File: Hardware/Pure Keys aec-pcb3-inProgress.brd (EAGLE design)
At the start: 99 x 98.7 mm, 61 parts, among them IC1 MCP6004P, IC5 MCP6004P, Q2 20MHz, T1 2N3904, U2 LM4040, U3 328P

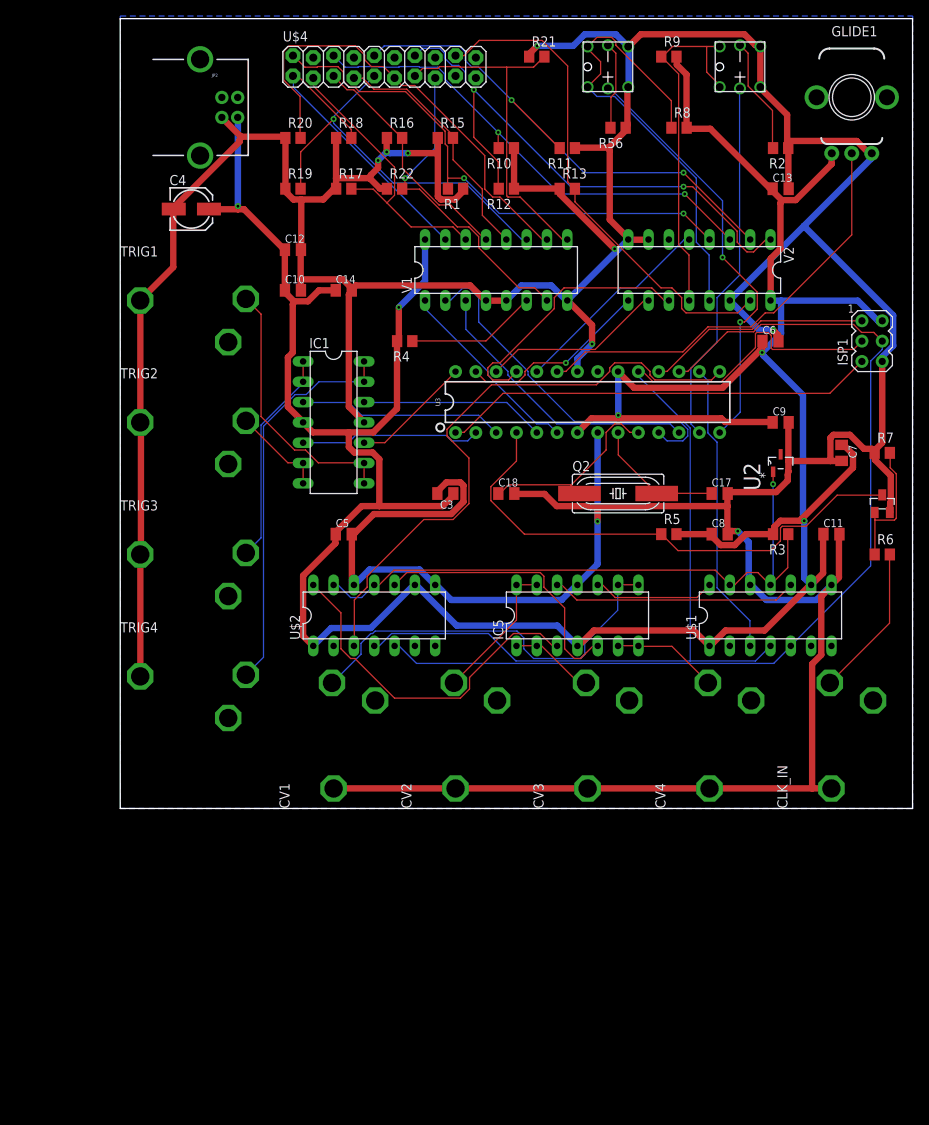
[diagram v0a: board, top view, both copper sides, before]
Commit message: adding part numbers to attributes
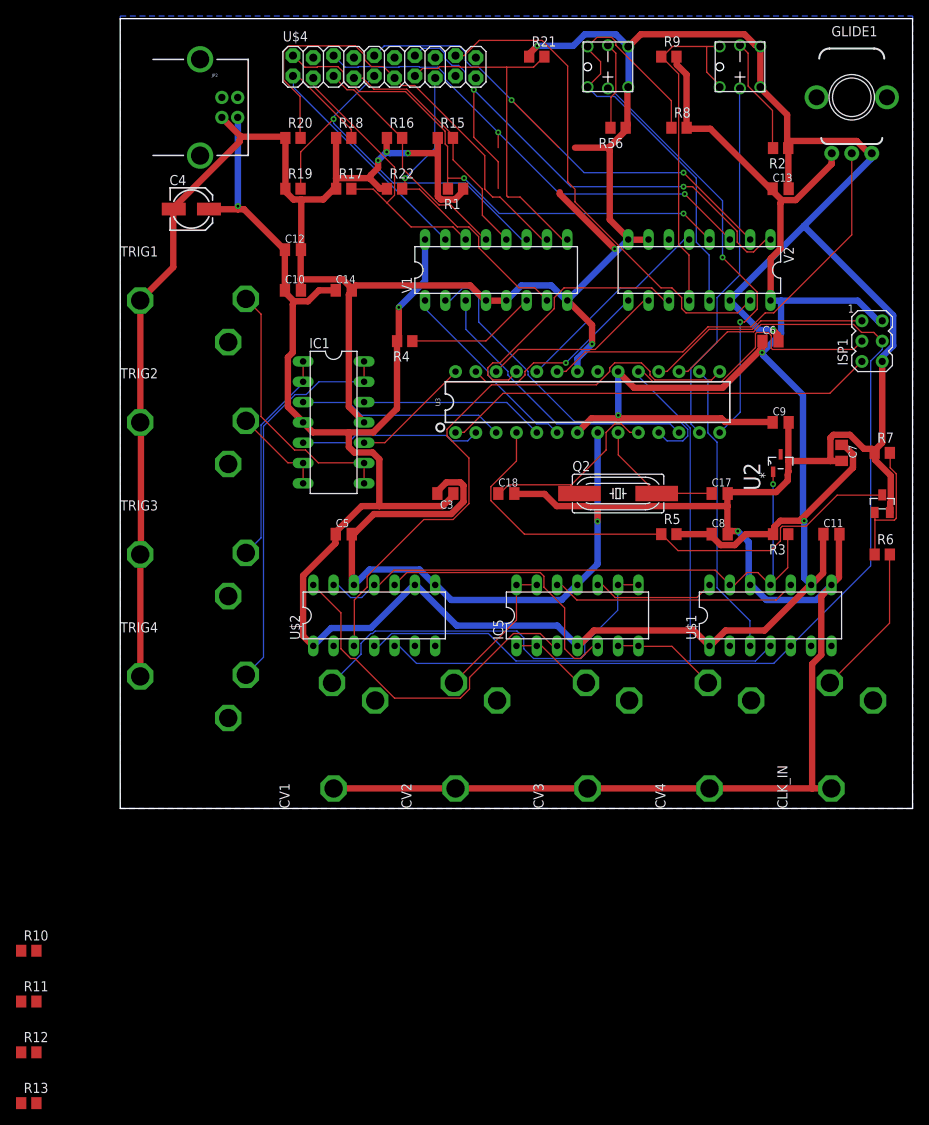
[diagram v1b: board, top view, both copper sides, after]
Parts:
- moved R13 132.6 mm to (-11.4, -36.8)
- moved R11 126.1 mm to (-11.4, -24.1), turned to 0 degrees
- moved R12 123.4 mm to (-11.4, -30.5), turned to 0 degrees
- moved R10 116.7 mm to (-11.4, -17.8), turned to 0 degrees
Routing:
- net GND: track 674.9 -> 663.6 mm
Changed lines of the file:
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@@
 <attribute name="OC_NEWARK" value="58K5870" x="82.55" y="43.18" size="1.778" layer="27" rot="R90" display="off"/>
 <attribute name="PACKAGE" value="3-SOT-23" x="82.55" y="43.18" size="1.778" layer="27" rot="R90" display="off"/>
+<attribute name="RS-PART" value="809-6343" x="82.55" y="43.18" size="1.778" layer="27" rot="R90" display="off"/>
 <attribute name="SUPPLIER" value="TEXAS INSTRUMENTS" x="82.55" y="43.18" size="1.778" layer="27" rot="R90" display="off"/>
 </element>
@@
 <element name="R8" library="rcl" package="R0805" value="100K" x="69.85" y="85.09"/>
 <element name="R9" library="rcl" package="R0805" value="100K" x="68.58" y="93.98"/>
-<element name="R1" library="rcl" package="R0805" value="1K" x="41.91" y="77.47" rot="R180"/>
-<element name="R10" library="rcl" package="R0805" value="1K" x="48.26" y="82.55" rot="R180"/>
-<element name="R11" library="rcl" package="R0805" value="1K" x="55.88" y="82.55" rot="R180"/>
-<element name="R12" library="rcl" package="R0805" value="1K" x="48.26" y="77.47" rot="R180"/>
-<element name="R13" library="rcl" package="R0805" value="1K" x="55.88" y="77.47"/>
+<element name="R1" library="rcl" package="R0805" value="1K" x="41.91" y="77.47" rot="R180">
+<attribute name="RS-PART" value="223-0427" x="41.91" y="77.47" size="1.778" layer="27" rot="R180" display="off"/>
+</element>
+<element name="R10" library="rcl" package="R0805" value="1K" x="-11.43" y="-17.78">
+<attribute name="RS-PART" value="223-0427" x="-11.43" y="-17.78" size="1.778" layer="27" display="off"/>
+</element>
+<element name="R11" library="rcl" package="R0805" value="1K" x="-11.43" y="-24.13">
+<attribute name="RS-PART" value="223-0427" x="-11.43" y="-24.13" size="1.778" layer="27" display="off"/>
+</element>
+<element name="R12" library="rcl" package="R0805" value="1K" x="-11.43" y="-30.48">
+<attribute name="RS-PART" value="223-0427" x="-11.43" y="-30.48" size="1.778" layer="27" display="off"/>
+</element>
+<element name="R13" library="rcl" package="R0805" value="1K" x="-11.43" y="-36.83">
+<attribute name="RS-PART" value="223-0427" x="-11.43" y="-36.83" size="1.778" layer="27" display="off"/>
+</element>
 </elements>
 <signals>
@@
 <contactref element="BUT2" pad="2"/>
 <contactref element="R1" pad="1"/>
-<contactref element="R10" pad="1"/>
-<contactref element="R11" pad="1"/>
-<contactref element="R12" pad="1"/>
-<contactref element="R13" pad="1"/>
 <wire x1="41.91" y1="2.5146" x2="26.67" y2="2.5146" width="0.8" layer="1"/>
 <wire x1="26.67" y1="2.5146" x2="26.67" y2="2.5" width="0.8" layer="1"/>
@@
 <wire x1="63.1698" y1="84.7344" x2="61.0362" y2="82.6008" width="0.8" layer="1"/>
 <wire x1="63.1698" y1="85.0392" x2="63.1698" y2="84.7344" width="0.8" layer="1"/>
-<wire x1="56.8452" y1="82.6008" x2="56.83" y2="82.55" width="0.8" layer="1"/>
 <wire x1="63.1698" y1="85.0392" x2="63.18" y2="85.09" width="0.8" layer="1"/>
 <wire x1="51.1302" y1="94.3356" x2="51.1302" y2="94.0308" width="0.8" layer="1"/>
@@
 <wire x1="63.5" y1="90.17" x2="63.3984" y2="90.0684" width="0.8" layer="1"/>
 <wire x1="63.3984" y1="85.4202" x2="63.18" y2="85.09" width="0.8" layer="1"/>
-<wire x1="49.2252" y1="82.5246" x2="49.2252" y2="77.4954" width="0.8" layer="1"/>
-<wire x1="49.2252" y1="77.4954" x2="49.21" y2="77.47" width="0.8" layer="1"/>
-<wire x1="49.2252" y1="82.5246" x2="49.21" y2="82.55" width="0.8" layer="1"/>
-<wire x1="49.6062" y1="77.4954" x2="54.864" y2="77.4954" width="0.8" layer="1"/>
-<wire x1="54.864" y1="77.4954" x2="54.93" y2="77.47" width="0.8" layer="1"/>
-<wire x1="49.6062" y1="77.4954" x2="49.21" y2="77.47" width="0.8" layer="1"/>
 <wire x1="65.9892" y1="71.0946" x2="63.5508" y2="71.0946" width="0.8" layer="1"/>
 <wire x1="63.5508" y1="71.0946" x2="63.5" y2="71.12" width="0.8" layer="1"/>
@@
 <wire x1="54.9402" y1="76.8096" x2="54.9402" y2="77.0382" width="0.8" layer="1"/>
 <wire x1="61.7982" y1="69.9516" x2="54.9402" y2="76.8096" width="0.8" layer="1"/>
-<wire x1="54.9402" y1="77.0382" x2="54.93" y2="77.47" width="0.8" layer="1"/>
 <wire x1="61.7982" y1="69.9516" x2="62.0649" y2="69.6849" width="0.8" layer="16"/>
 <wire x1="61.1886" y1="73.6092" x2="61.1886" y2="82.2198" width="0.8" layer="1"/>
@@
 <via x="32.2326" y="81.0006" extent="1-16" drill="0.35"/>
 <via x="35.9664" y="81.915" extent="1-16" drill="0.35"/>
+<contactref element="R10" pad="1"/>
+<contactref element="R11" pad="1"/>
+<contactref element="R12" pad="1"/>
+<contactref element="R13" pad="1"/>
+<wire x1="-12.38" y1="-30.48" x2="-12.38" y2="-36.83" width="0" layer="19" extent="1-1"/>
+<wire x1="-12.38" y1="-24.13" x2="-12.38" y2="-30.48" width="0" layer="19" extent="1-1"/>
+<wire x1="-12.38" y1="-17.78" x2="-12.38" y2="-24.13" width="0" layer="19" extent="1-1"/>
+<wire x1="2.5" y1="16.51" x2="-12.38" y2="-17.78" width="0" layer="19" extent="1-1"/>
 </signal>
 <signal name="RST">
@@
 <contactref element="V2" pad="15"/>
 <contactref element="U$4" pad="18"/>
-<contactref element="R13" pad="2"/>
 <wire x1="56.8452" y1="75.819" x2="56.8452" y2="77.4192" width="0.1524" layer="1"/>
 <wire x1="67.5894" y1="65.0748" x2="56.8452" y2="75.819" width="0.1524" layer="1"/>
@@
 <wire x1="77.1906" y1="61.9506" x2="70.7136" y2="61.9506" width="0.1524" layer="1"/>
 <wire x1="78.74" y1="63.5" x2="77.1906" y2="61.9506" width="0.1524" layer="1"/>
-<wire x1="56.8452" y1="77.4192" x2="56.83" y2="77.47" width="0.1524" layer="1"/>
 <wire x1="42.9768" y1="94.107" x2="41.91" y2="94.107" width="0.1524" layer="1"/>
 <wire x1="44.8818" y1="96.012" x2="42.9768" y2="94.107" width="0.1524" layer="1"/>
@@
 <wire x1="55.9308" y1="78.3336" x2="55.9308" y2="92.8116" width="0.1524" layer="1"/>
 <wire x1="56.769" y1="77.4954" x2="55.9308" y2="78.3336" width="0.1524" layer="1"/>
-<wire x1="56.769" y1="77.4954" x2="56.83" y2="77.47" width="0.1524" layer="1"/>
+<contactref element="R13" pad="2"/>
+<wire x1="56.8452" y1="77.4192" x2="56.769" y2="77.4954" width="0" layer="19" extent="1-1"/>
+<wire x1="-10.48" y1="-36.83" x2="70.7136" y2="61.9506" width="0" layer="19" extent="1-1"/>
 </signal>
 <signal name="MK3">
 <contactref element="U$4" pad="14"/>
-<contactref element="R12" pad="2"/>
 <contactref element="V2" pad="1"/>
 <wire x1="47.244" y1="80.8482" x2="47.244" y2="77.4954" width="0.1524" layer="1"/>
@@
 <wire x1="37.7952" y1="95.0214" x2="39.9288" y2="95.0214" width="0.1524" layer="16"/>
 <wire x1="36.8808" y1="94.107" x2="37.7952" y2="95.0214" width="0.1524" layer="16"/>
-<wire x1="47.244" y1="77.4954" x2="47.31" y2="77.47" width="0.1524" layer="1"/>
 <wire x1="36.8808" y1="94.107" x2="36.83" y2="94.107" width="0.1524" layer="16"/>
 <wire x1="80.6958" y1="71.0946" x2="81.2292" y2="71.0946" width="0.1524" layer="1"/>
@@
 <via x="44.196" y="89.8398" extent="1-16" drill="0.35"/>
 <via x="70.4088" y="77.724" extent="1-16" drill="0.35"/>
+<contactref element="R12" pad="2"/>
+<wire x1="-10.48" y1="-30.48" x2="47.244" y2="77.4954" width="0" layer="19" extent="1-1"/>
 </signal>
 <signal name="MK2">
 <contactref element="U$4" pad="10"/>
-<contactref element="R11" pad="2"/>
 <contactref element="V2" pad="2"/>
 <wire x1="48.9204" y1="88.5444" x2="54.864" y2="82.6008" width="0.1524" layer="1"/>
@@
 <wire x1="32.9946" y1="95.3262" x2="42.3672" y2="95.3262" width="0.1524" layer="16"/>
 <wire x1="31.7754" y1="94.107" x2="32.9946" y2="95.3262" width="0.1524" layer="16"/>
-<wire x1="54.864" y1="82.6008" x2="54.93" y2="82.55" width="0.1524" layer="1"/>
 <wire x1="31.7754" y1="94.107" x2="31.75" y2="94.107" width="0.1524" layer="16"/>
 <wire x1="70.4088" y1="79.4766" x2="78.7146" y2="71.1708" width="0.1524" layer="1"/>
@@
 <via x="48.9204" y="88.5444" extent="1-16" drill="0.35"/>
 <via x="70.4088" y="79.4766" extent="1-16" drill="0.35"/>
+<contactref element="R11" pad="2"/>
+<wire x1="-10.48" y1="-24.13" x2="57.9882" y2="79.4766" width="0" layer="19" extent="1-16"/>
 </signal>
 <signal name="TRIG3">
@@
 <signal name="MK1">
 <contactref element="U$4" pad="6"/>
-<contactref element="R10" pad="2"/>
 <contactref element="V2" pad="3"/>
 <wire x1="47.244" y1="84.5058" x2="47.244" y2="82.6008" width="0.1524" layer="1"/>
@@
 <wire x1="28.1178" y1="92.6592" x2="29.718" y2="92.6592" width="0.1524" layer="16"/>
 <wire x1="26.67" y1="94.107" x2="28.1178" y2="92.6592" width="0.1524" layer="16"/>
-<wire x1="47.244" y1="82.6008" x2="47.31" y2="82.55" width="0.1524" layer="1"/>
 <wire x1="70.5612" y1="76.8096" x2="76.2" y2="71.1708" width="0.1524" layer="1"/>
 <wire x1="54.9402" y1="76.8096" x2="70.5612" y2="76.8096" width="0.1524" layer="16"/>
@@
 <via x="47.244" y="84.5058" extent="1-16" drill="0.35"/>
 <via x="70.5612" y="76.8096" extent="1-16" drill="0.35"/>
+<contactref element="R10" pad="2"/>
+<wire x1="-10.48" y1="-17.78" x2="54.9402" y2="76.8096" width="0" layer="19" extent="1-16"/>
 </signal>
 <signal name="MK0">

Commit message: routing on pcb-3-inprogress
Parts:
- U$4: device SparkFun-Connectors:2X10_LOCK -> SparkFun-Connectors:2X10
- moved R12 132.0 mm to (54.6, 83.8)
- moved R13 132.0 mm to (54.6, 77.5)
- moved R10 117.8 mm to (48.3, 83.8)
- moved R11 117.8 mm to (48.3, 77.5)
- moved U$4 10.2 mm to (22.9, 92.7)
- moved R2 5.24 mm to (77.5, 83.8)
- moved R21 2.54 mm to (52.1, 91.4)
- moved R56 1.27 mm to (62.2, 83.8)
- moved R8 1.27 mm to (69.8, 83.8)
- moved R1 1.27 mm to (40.6, 77.5)
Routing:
- net 5V: track 400.0 -> 419.8 mm, vias 5 -> 6
- net MK0: track 66.9 -> 83.2 mm, vias 2 -> 1
- net BUT1: track 58.6 -> 42.6 mm, vias 0 -> 1
- net T7: track 40.5 -> 54.0 mm, vias 1 -> 0
- net MK3: track 71.4 -> 58.5 mm
- net T2: track 29.8 -> 40.9 mm
- net A0IN: track 33.5 -> 22.8 mm
- net T0: track 39.5 -> 29.0 mm, vias 0 -> 1
- net VOUTC: track 43.8 -> 33.6 mm
- net GND: track 663.6 -> 653.4 mm, vias 9 -> 5
- net T1: track 37.1 -> 45.9 mm
- net CS2: track 75.7 -> 67.1 mm, vias 0 -> 1
- net MK4: track 62.5 -> 55.2 mm, vias 0 -> 1
- net A0OUT: track 24.2 -> 30.6 mm, vias 0 -> 1
- net T4: track 48.6 -> 55.0 mm
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- removed copper zone on layer 16, net N$1
